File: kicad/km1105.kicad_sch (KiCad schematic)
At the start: 37 parts, among them J2 display_switches_hdr, J3 pgm_hdr, J9 DEC-FLIP-CHIP_CONN-DEC-DOUBLE, Q1 BC547, U1 ATtiny1616-S, U2 PCF8574T, U3 PCF8574T, U4 PCF8574T, U5 PCF8574T, U6 PCF8574T, U7 PCF8574T, U8 74ACT00SC, U9 LD1117S33TR_SOT223

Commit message: Finished PCB with oddities removed
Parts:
- removed J9: DEC-FLIP-CHIP_CONN-DEC-DOUBLE, DEC-FLIP-CHIP:CONN-DEC-DOUBLE, symbol frits:DEC-FLIP-CHIP_CONN-DEC-DOUBLE
- added H1, H2, H3, H4: (no value), MountingHole:MountingHole_3.2mm_M3, symbol Mechanical:MountingHole
- added J1: CONN-DEC-DOUBLE, DEC-FLIP-CHIP:CONN-DEC-DOUBLE, symbol DEC-FLIP-CHIP:CONN-DEC-DOUBLE
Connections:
- net +5V: now also J1.AA2, J1.BA2
- net 8V: now also J1.AB1
- net 8V_2: now also J1.BB1
- net BSR0_H: now also J1.AR2
- net BSR0_H_2: now also J1.BR2
- net BSR12_H: now also J1.AH2
- net BSR12_H_2: now also J1.BH2
- net BSR14_H: now also J1.AD2
- net BSR14_H_2: now also J1.BD2
- net BSR15_H: now also J1.AN2
- net BSR15_H_2: now also J1.BN2
- net BSR1_H: now also J1.AE2
- net BSR1_H_2: now also J1.BE2
- net BSR3_H: now also J1.AH1
- net BSR3_H_2: now also J1.BH1
- net BSR7_H: now also J1.AL2
- net BSR7_H_2: now also J1.BL2
- net BSR8_H: now also J1.AJ2
- net BSR8_H_2: now also J1.BJ2
- net BUS_SSYN_L: now also J1.AA1
- net BUS_SSYN_L_2: now also J1.BA1
- net B_MSYN_H: now also J1.AT2
- net B_MSYN_H_2: now also J1.BT2
- net B_SSYN_H: now also J1.AU2
- net B_SSYN_H_2: now also J1.BU2
- net C_H: now also J1.AD1
- net C_H_2: now also J1.BD1
- net GND: now also J1.AC2, J1.AT1, J1.BC2, J1.BT1
- net ISR0_H: now also J1.AS1
- net ISR0_H_2: now also J1.BS1
- net ISR12_H: now also J1.AS2
- net ISR12_H_2: now also J1.BS2
- net ISR14_H: now also J1.AK1
- net ISR14_H_2: now also J1.BK1
- net ISR15_H: now also J1.AR1
- net ISR15_H_2: now also J1.BR1
- net ISR1_H: now also J1.AM2
- net ISR1_H_2: now also J1.BM2
- net ISR2_H: now also J1.AP2
- net ISR2_H_2: now also J1.BP2
- net ISR3_H: now also J1.AF2
- net ISR3_H_2: now also J1.BF2
- net ISR7_H: now also J1.AE1
- net ISR7_H_2: now also J1.BE1
- net ISR8_H: now also J1.AM1
- net ISR8_H_2: now also J1.BM1
- net M_CLK_ENABLE_L: now also J1.AV2
- net M_CLK_ENABLE_L_2: now also J1.BV2
- net M_CLK_L: now also J1.AU1
- net M_CLK_L_2: now also J1.BU1
- net N_H: now also J1.AP1
- net N_H_2: now also J1.BP1
- net RW2_H: now also J1.AK2
- net RW2_H_2: now also J1.BK2
- net TIMEOUT_H: now also J1.AB2
- net TIMEOUT_H_2: now also J1.BB2
- net TRAPS_H: now also J1.AC1
- net TRAPS_H_2: now also J1.BC1
- net TST1_H: now also J1.AN1
- net TST1_H_2: now also J1.BN1
- net TST2_H: now also J1.AV1
- net TST2_H_2: now also J1.BV1
- net T_H: now also J1.AJ1
- net T_H_2: now also J1.BJ1
- net V_H: now also J1.AF1
- net V_H_2: now also J1.BF1
- net Z_H: now also J1.AL1
- net Z_H_2: now also J1.BL1
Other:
- company: (none) -> ErrorSoft
- title: (none) -> pdp 11/05 KM11 double module w/LCD

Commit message: Implement expanders and read the signals
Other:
- note added: "alum"
- note added: "aux_c*"
- note added: "but_jj*"
- note added: "but_un*"
- note added: "cin"
- note added: "cnst*"
- note added: "ealu"
- note added: "mpc*0..7 (km1)"
- note added: "spad0..3, alu*_s0..3 (km2)"
- note added: "spwr"
- note removed: "mcp0..7 (km1)"
- note removed: "spad0..3, alu_s0..3 (km2)"
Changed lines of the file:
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@@
 		(company "ErrorSoft")
+	)
+	(text "cin"
+		(exclude_from_sim no)
+		(at 153.924 74.168 0)
+		(effects
+			(font
+				(size 1.27 1.27)
+			)
+		)
+	)
+	(text "but_un*"
+		(exclude_from_sim no)
+		(at 157.226 98.552 0)
+		(effects
+			(font
+				(size 1.27 1.27)
+			)
+		)
 	)
 	(text "km2: c1*"
@@
 		)
 	)
+	(text "but_jj*"
+		(exclude_from_sim no)
+		(at 156.464 101.092 0)
+		(effects
+			(font
+				(size 1.27 1.27)
+			)
+		)
+	)
 	(text "amux8..15 (km1)"
 		(exclude_from_sim no)
 		(at 100.584 88.9 0)
+		(effects
+			(font
+				(size 1.27 1.27)
+			)
+		)
+	)
+	(text "spwr"
+		(exclude_from_sim no)
+		(at 155.194 69.088 0)
+		(effects
+			(font
+				(size 1.27 1.27)
+			)
+		)
+	)
+	(text "ealu"
+		(exclude_from_sim no)
+		(at 155.194 71.882 0)
+		(effects
+			(font
+				(size 1.27 1.27)
+			)
+		)
+	)
+	(text "alum"
+		(exclude_from_sim no)
+		(at 154.686 76.708 0)
 		(effects
 			(font
@@
 		)
 	)
-	(text "spad0..3, alu_s0..3 (km2)"
+	(text "spad0..3, alu*_s0..3 (km2)"
 		(exclude_from_sim no)
 		(at 147.066 16.51 0)
@@
 		)
 	)
-	(text "mcp0..7 (km1)"
+	(text "aux_c*"
+		(exclude_from_sim no)
+		(at 156.718 103.378 0)
+		(effects
+			(font
+				(size 1.27 1.27)
+			)
+		)
+	)
+	(text "mpc*0..7 (km1)"
 		(exclude_from_sim no)
 		(at 100.076 16.51 0)
 		(effects
 			(font
+				(size 1.27 1.27)
+			)
+		)
+	)
+	(text "cnst*"
+		(exclude_from_sim no)
+		(at 155.956 95.758 0)
+		(effects
+			(font

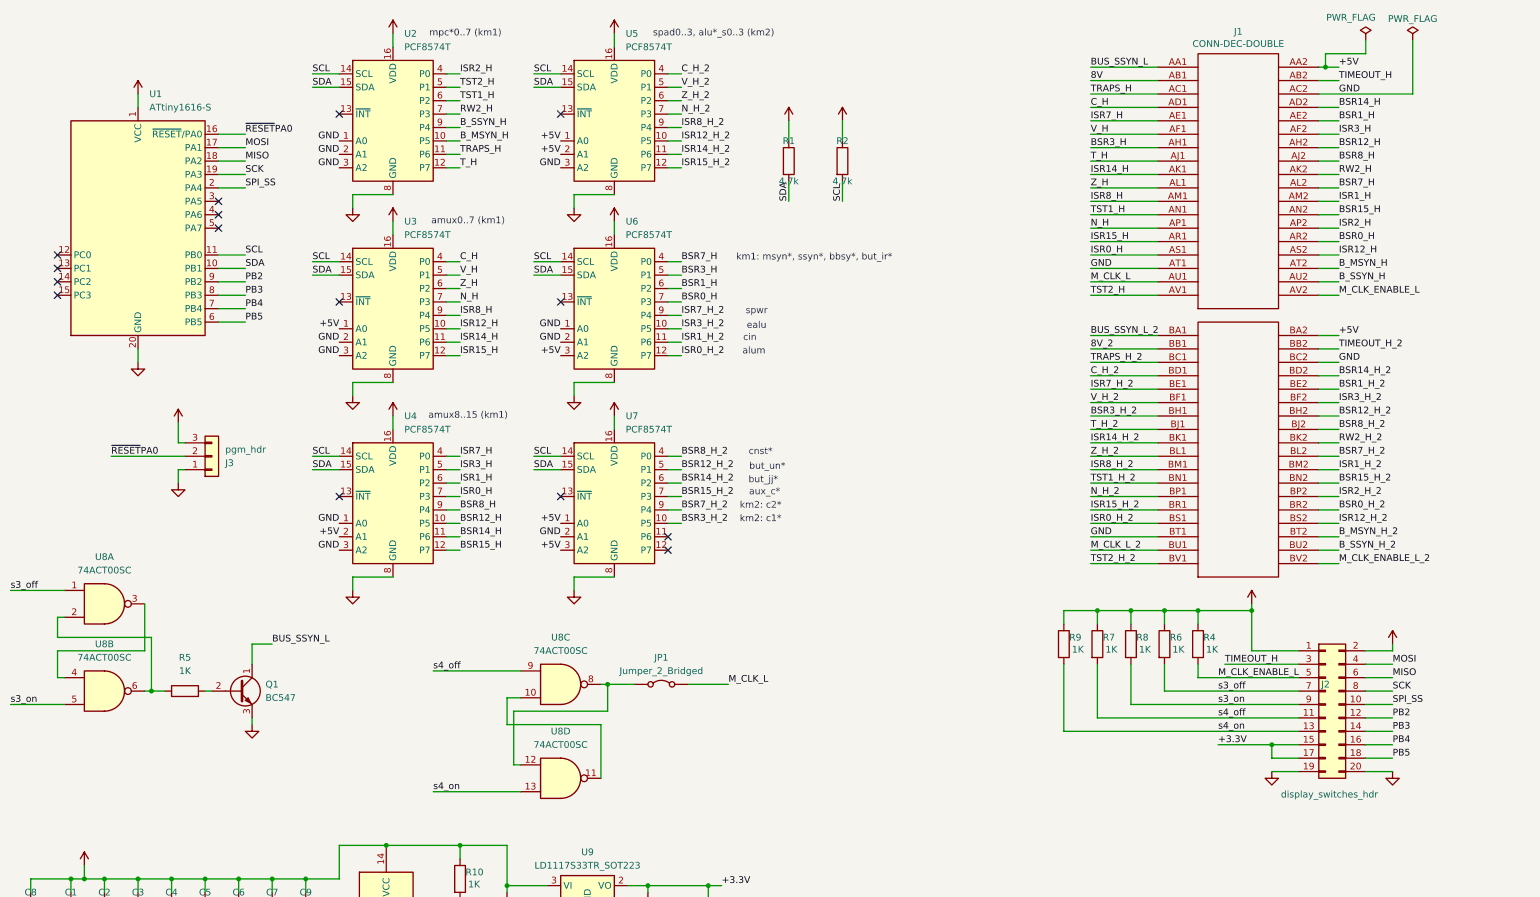
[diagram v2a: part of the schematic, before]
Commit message: Add a larger font, reformat screen, fix signal names on schematic
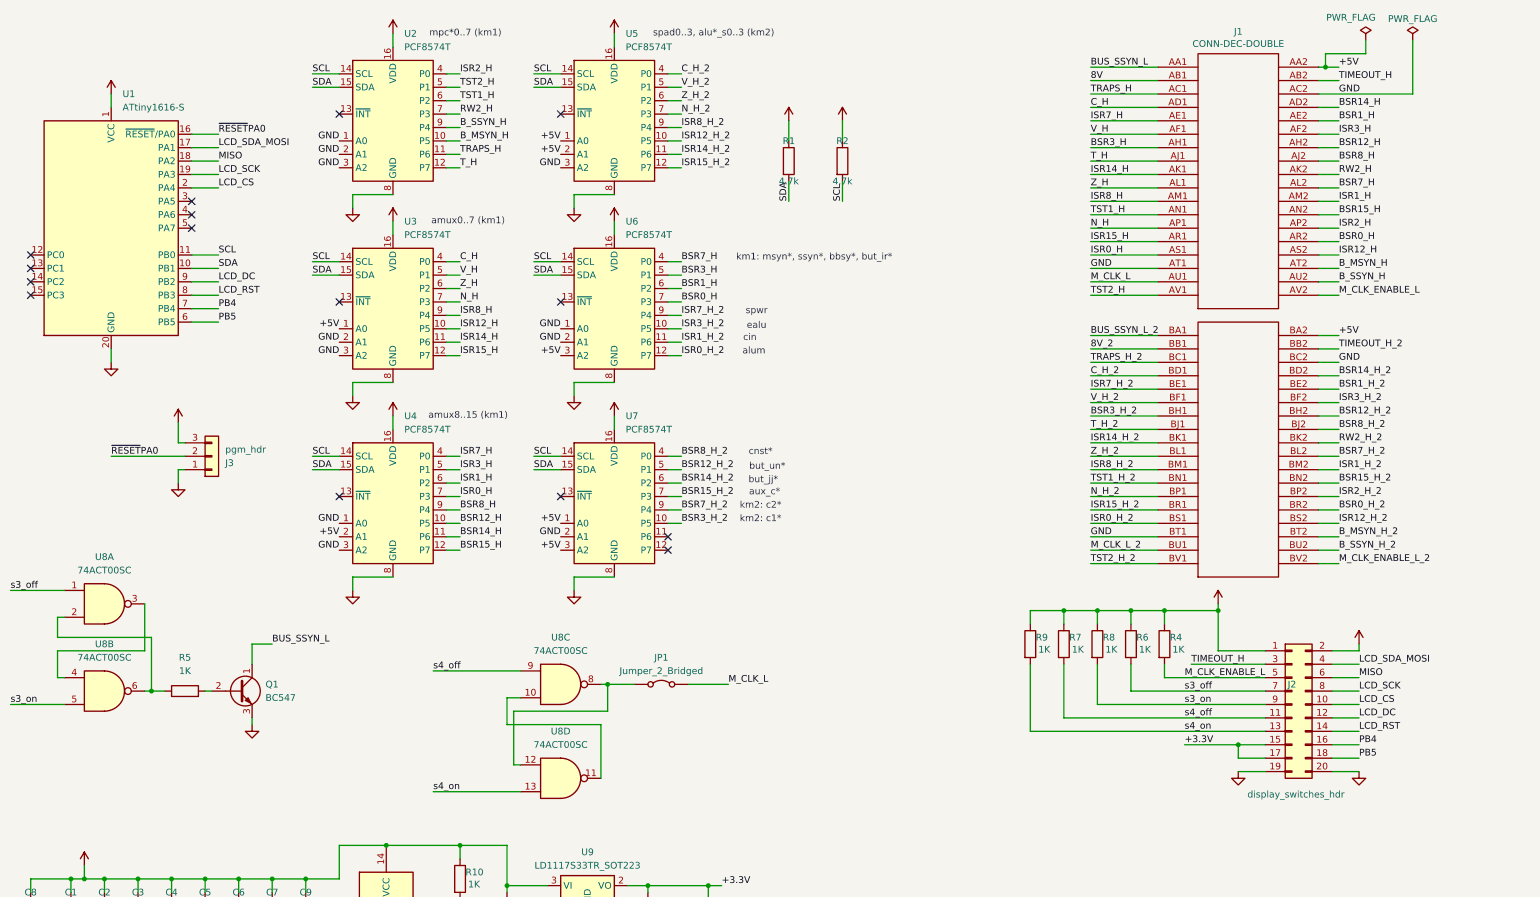
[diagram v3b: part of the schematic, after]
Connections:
- net MOSI renamed LCD_SDA_MOSI
- net PB2 renamed LCD_DC
- net PB3 renamed LCD_RST
- net SCK renamed LCD_SCK
- net SPI_SS renamed LCD_CS
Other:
- moved on the sheet: J2, R4, R6, R7, R8, R9, U1

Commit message: Bugfixes and 3d printed box
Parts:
- U8: footprint Package_SO:SOIC-14W_7.5x9mm_P1.27mm -> Package_SO:SO-14_3.9x8.65mm_P1.27mm
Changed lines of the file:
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@@
 			)
 		)
-		(property "Footprint" "Package_SO:SOIC-14W_7.5x9mm_P1.27mm"
+		(property "Footprint" "Package_SO:SO-14_3.9x8.65mm_P1.27mm"
 			(at 31.75 124.46 0)
 			(hide yes)
@@
 			)
 		)
-		(property "Footprint" "Package_SO:SOIC-14W_7.5x9mm_P1.27mm"
+		(property "Footprint" "Package_SO:SO-14_3.9x8.65mm_P1.27mm"
 			(at 118.11 157.48 0)
 			(hide yes)
@@
 			)
 		)
-		(property "Footprint" "Package_SO:SOIC-14W_7.5x9mm_P1.27mm"
+		(property "Footprint" "Package_SO:SO-14_3.9x8.65mm_P1.27mm"
 			(at 31.75 140.97 0)
 			(hide yes)
@@
 			)
 		)
-		(property "Footprint" "Package_SO:SOIC-14W_7.5x9mm_P1.27mm"
+		(property "Footprint" "Package_SO:SO-14_3.9x8.65mm_P1.27mm"
 			(at 85.09 182.88 0)
 			(hide yes)
@@
 			)
 		)
-		(property "Footprint" "Package_SO:SOIC-14W_7.5x9mm_P1.27mm"
+		(property "Footprint" "Package_SO:SO-14_3.9x8.65mm_P1.27mm"
 			(at 118.11 139.7 0)
 			(hide yes)
